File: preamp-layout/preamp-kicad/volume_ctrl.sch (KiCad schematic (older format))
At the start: 64 parts, among them J64 Conn_01x05_Male, J65 Conn_01x02_Male, J66 Conn_01x02_Male, J67 Conn_01x03_Female, J68 Conn_01x03_Female, J69 Conn_01x03_Male, J70 Conn_01x03_Male, J71 Conn_01x03_Male, U10 MCP4902, U11 TL072, U12 TL072, U13 THAT2181, U14 THAT2181, U15 TL072, U16 THAT2181, U17 THAT2181, U18 TL072, U9 MCP4902

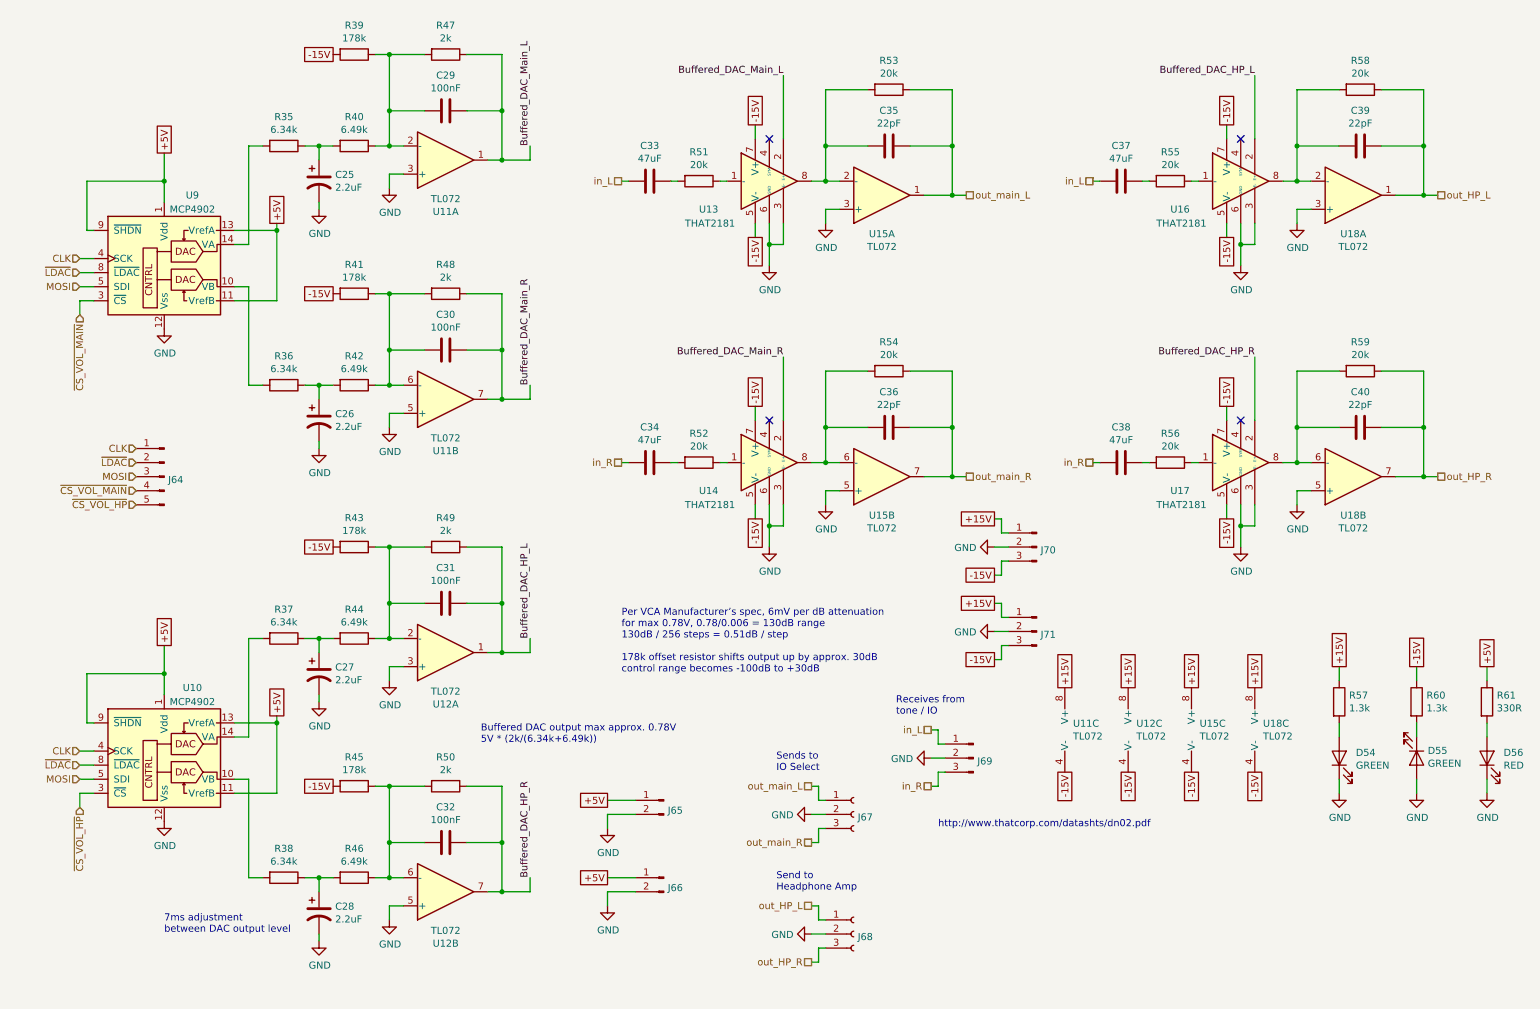
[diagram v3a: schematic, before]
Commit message: Schematic Redesignation
Regenerated RefDes for all parts, updated BOM accordingly and perfomred check on values, RefDes present from schematic to BOM. Value changes, BOM filled in as a result.
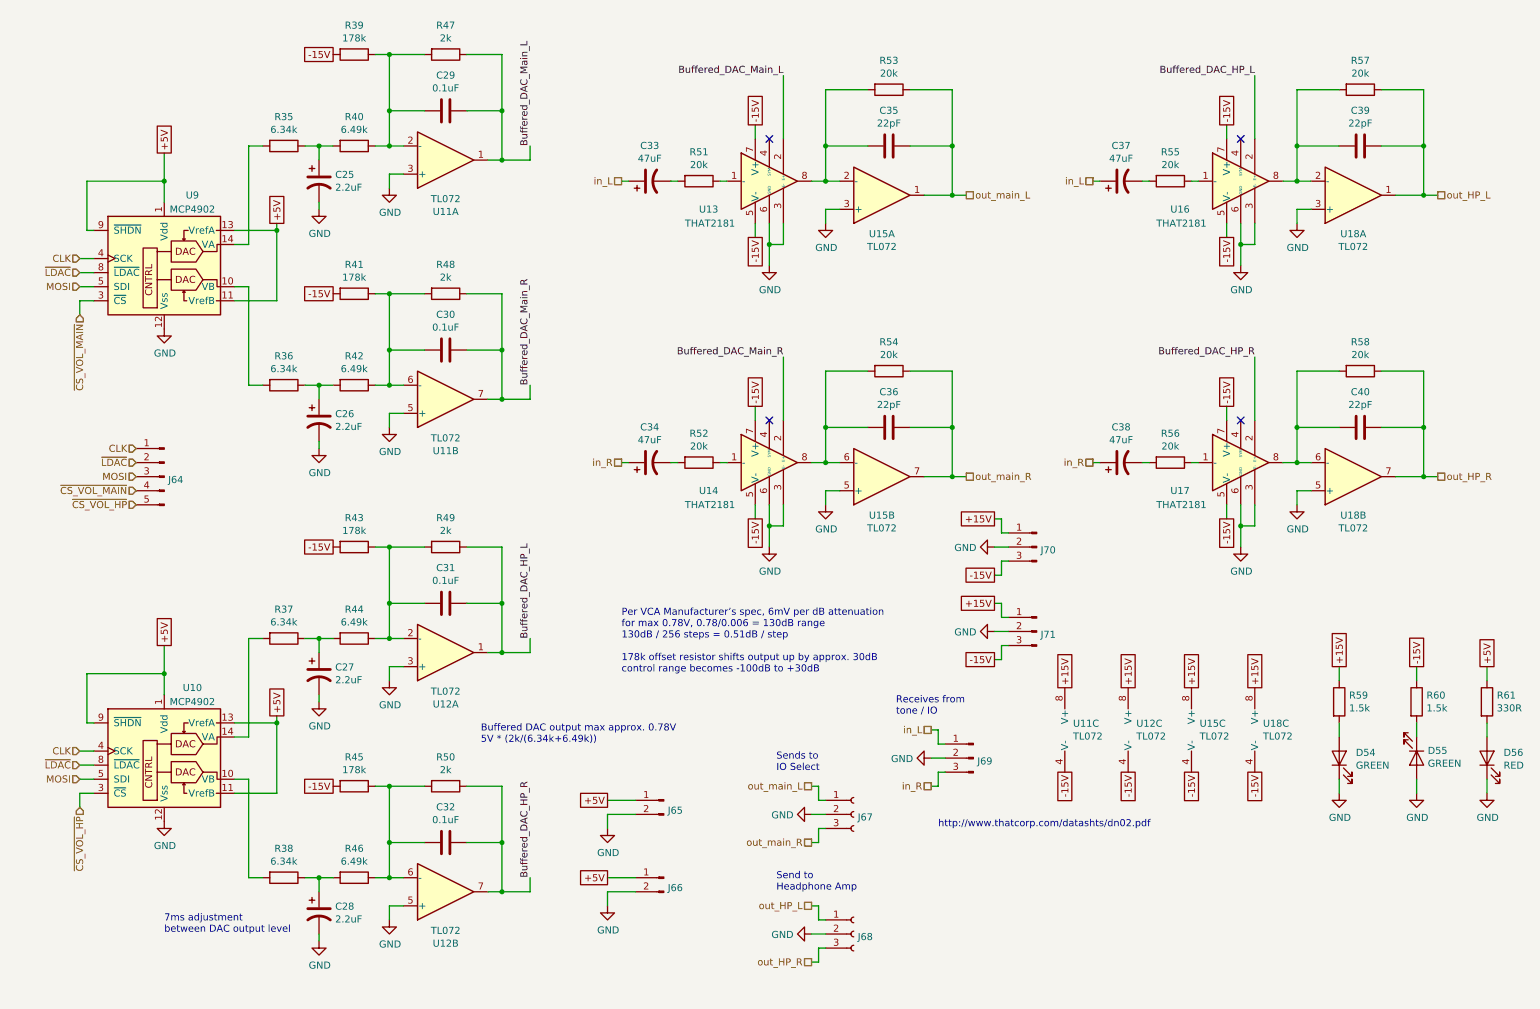
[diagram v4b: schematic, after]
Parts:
- removed C33, C34, C37, C38: 47uF, symbol Device:C
- added C33, C34, C37, C38: 47uF, symbol Device:CP1
- C29, C30, C31, C32: value 100nF -> 0.1uF
- R59: renamed from R57; value 1.3k -> 1.5k
- R60: value 1.3k -> 1.5k
- renumbered R58 to R57, R59 to R58
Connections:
- net in_L: now also C33.1, C37.1
- net in_R: now also C34.1, C38.1
- net at R51.2: now also C33.2
- net at R52.2: now also C34.2
- net at R55.2: now also C37.2
- net at R56.2: now also C38.2
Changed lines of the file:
@@
-	0    1    1    0
-$EndComp
-$Comp
-L Device:C C?
-U 1 1 600B8889
-P 3500 1400
-AR Path="/61DC5D9D/600B8889" Ref="C?"  Part="1"
-AR Path="/5F2E428C/600B8889" Ref="C?"  Part="1"
-AR Path="/61DA059E/600B8889" Ref="C?"  Part="1"
-AR Path="/6009D432/600B8889" Ref="C29"  Part="1"
-F 0 "C29" V 3248 1400 50  0000 C CNN
-F 1 "100nF" V 3339 1400 50  0000 C CNN
-F 2 "Capacitor_SMD:C_0805_2012Metric_Pad1.15x1.40mm_HandSolder" H 3538 1250 50  0001 C CNN
-F 3 "~" H 3500 1400 50  0001 C CNN
-	1    3500 1400
 	0    1    1    0
 $EndComp
@@
 F 3 "~" H 5300 1900 50  0001 C CNN
 	1    5300 1900
-	0    1    1    0
-$EndComp
-$Comp
-L Device:C C?
-U 1 1 60191212
-P 4950 1900
-AR Path="/61DC5D9D/60191212" Ref="C?"  Part="1"
-AR Path="/5F2E428C/60191212" Ref="C?"  Part="1"
-AR Path="/61DA059E/60191212" Ref="C?"  Part="1"
-AR Path="/6009D432/60191212" Ref="C33"  Part="1"
-F 0 "C33" V 4698 1900 50  0000 C CNN
-F 1 "47uF" V 4789 1900 50  0000 C CNN
-F 2 "" H 4988 1750 50  0001 C CNN
-F 3 "~" H 4950 1900 50  0001 C CNN
-	1    4950 1900
 	0    1    1    0
 $EndComp
@@
 AR Path="/6009D432/60205A00" Ref="C30"  Part="1"
 F 0 "C30" V 3248 3100 50  0000 C CNN
-F 1 "100nF" V 3339 3100 50  0000 C CNN
+F 1 "0.1uF" V 3339 3100 50  0000 C CNN
 F 2 "Capacitor_SMD:C_0805_2012Metric_Pad1.15x1.40mm_HandSolder" H 3538 2950 50  0001 C CNN
 F 3 "~" H 3500 3100 50  0001 C CNN
@@
 $EndComp
 $Comp
-L Device:C C?
-U 1 1 602F6E88
-P 4950 3900
-AR Path="/61DC5D9D/602F6E88" Ref="C?"  Part="1"
-AR Path="/5F2E428C/602F6E88" Ref="C?"  Part="1"
-AR Path="/61DA059E/602F6E88" Ref="C?"  Part="1"
-AR Path="/6009D432/602F6E88" Ref="C34"  Part="1"
-F 0 "C34" V 4698 3900 50  0000 C CNN
-F 1 "47uF" V 4789 3900 50  0000 C CNN
-F 2 "" H 4988 3750 50  0001 C CNN
-F 3 "~" H 4950 3900 50  0001 C CNN
-	1    4950 3900
-	0    1    1    0
-$EndComp
-$Comp
 L Amplifier_Audio:THAT2181 U14
 U 1 1 602F6E92
@@
 AR Path="/6009D432/6033B910" Ref="C31"  Part="1"
 F 0 "C31" V 3248 4900 50  0000 C CNN
-F 1 "100nF" V 3339 4900 50  0000 C CNN
+F 1 "0.1uF" V 3339 4900 50  0000 C CNN
 F 2 "Capacitor_SMD:C_0805_2012Metric_Pad1.15x1.40mm_HandSolder" H 3538 4750 50  0001 C CNN
 F 3 "~" H 3500 4900 50  0001 C CNN
@@
 $EndComp
 $Comp
-L Device:C C?
-U 1 1 6033B963
-P 8300 1900
-AR Path="/61DC5D9D/6033B963" Ref="C?"  Part="1"
-AR Path="/5F2E428C/6033B963" Ref="C?"  Part="1"
-AR Path="/61DA059E/6033B963" Ref="C?"  Part="1"
-AR Path="/6009D432/6033B963" Ref="C37"  Part="1"
-F 0 "C37" V 8048 1900 50  0000 C CNN
-F 1 "47uF" V 8139 1900 50  0000 C CNN
-F 2 "" H 8338 1750 50  0001 C CNN
-F 3 "~" H 8300 1900 50  0001 C CNN
-	1    8300 1900
-	0    1    1    0
-$EndComp
-$Comp
 L Amplifier_Audio:THAT2181 U16
 U 1 1 6033B96D
@@
 P 10000 1250
 AR Path="/61DA059E/6033B977" Ref="R?"  Part="1"
-AR Path="/6009D432/6033B977" Ref="R58"  Part="1"
-F 0 "R58" V 9793 1250 50  0000 C CNN
+AR Path="/6009D432/6033B977" Ref="R57"  Part="1"
+F 0 "R57" V 9793 1250 50  0000 C CNN
 F 1 "20k" V 9884 1250 50  0000 C CNN
 F 2 "Resistor_SMD:R_1206_3216Metric_Pad1.42x1.75mm_HandSolder" V 9930 1250 50  0001 C CNN
@@
 AR Path="/6009D432/6033B9D4" Ref="C32"  Part="1"
 F 0 "C32" V 3248 6600 50  0000 C CNN
-F 1 "100nF" V 3339 6600 50  0000 C CNN
+F 1 "0.1uF" V 3339 6600 50  0000 C CNN
 F 2 "Capacitor_SMD:C_0805_2012Metric_Pad1.15x1.40mm_HandSolder" H 3538 6450 50  0001 C CNN
 F 3 "~" H 3500 6600 50  0001 C CNN
@@
 $EndComp
 $Comp
-L Device:C C?
-U 1 1 6033BA6E
-P 8300 3900
-AR Path="/61DC5D9D/6033BA6E" Ref="C?"  Part="1"
-AR Path="/5F2E428C/6033BA6E" Ref="C?"  Part="1"
-AR Path="/61DA059E/6033BA6E" Ref="C?"  Part="1"
-AR Path="/6009D432/6033BA6E" Ref="C38"  Part="1"
-F 0 "C38" V 8048 3900 50  0000 C CNN
-F 1 "47uF" V 8139 3900 50  0000 C CNN
-F 2 "" H 8338 3750 50  0001 C CNN
-F 3 "~" H 8300 3900 50  0001 C CNN
-	1    8300 3900
-	0    1    1    0
-$EndComp
-$Comp
 L Amplifier_Audio:THAT2181 U17
 U 1 1 6033BA78
@@
 P 10000 3250
 AR Path="/61DA059E/6033BA82" Ref="R?"  Part="1"
-AR Path="/6009D432/6033BA82" Ref="R59"  Part="1"
-F 0 "R59" V 9793 3250 50  0000 C CNN
+AR Path="/6009D432/6033BA82" Ref="R58"  Part="1"
+F 0 "R58" V 9793 3250 50  0000 C CNN
 F 1 "20k" V 9884 3250 50  0000 C CNN
 F 2 "Resistor_SMD:R_1206_3216Metric_Pad1.42x1.75mm_HandSolder" V 9930 3250 50  0001 C CNN
@@
 AR Path="/6072D4FD" Ref="R?"  Part="1"
 AR Path="/5E27B612/6072D4FD" Ref="R?"  Part="1"
-AR Path="/6009D432/6072D4FD" Ref="R57"  Part="1"
-F 0 "R57" H 9920 5646 50  0000 L CNN
-F 1 "1.3k" H 9920 5555 50  0000 L CNN
+AR Path="/6009D432/6072D4FD" Ref="R59"  Part="1"
+F 0 "R59" H 9920 5646 50  0000 L CNN
+F 1 "1.5k" H 9920 5555 50  0000 L CNN
 F 2 "Resistor_SMD:R_1206_3216Metric_Pad1.42x1.75mm_HandSolder" V 9780 5600 50  0001 C CNN
 F 3 "~" H 9850 5600 50  0001 C CNN
@@
 AR Path="/6009D432/6072D50D" Ref="R60"  Part="1"
 F 0 "R60" H 10470 5646 50  0000 L CNN
-F 1 "1.3k" H 10470 5555 50  0000 L CNN
+F 1 "1.5k" H 10470 5555 50  0000 L CNN
 F 2 "Resistor_SMD:R_1206_3216Metric_Pad1.42x1.75mm_HandSolder" V 10330 5600 50  0001 C CNN
 F 3 "~" H 10400 5600 50  0001 C CNN
@@
 Wire Wire Line
 	900  2750 1000 2750
+$Comp
+L Device:C C?
+U 1 1 600B8889
+P 3500 1400
+AR Path="/61DC5D9D/600B8889" Ref="C?"  Part="1"
+AR Path="/5F2E428C/600B8889" Ref="C?"  Part="1"
+AR Path="/61DA059E/600B8889" Ref="C?"  Part="1"
+AR Path="/6009D432/600B8889" Ref="C29"  Part="1"
+F 0 "C29" V 3248 1400 50  0000 C CNN
+F 1 "0.1uF" V 3339 1400 50  0000 C CNN
+F 2 "Capacitor_SMD:C_0805_2012Metric_Pad1.15x1.40mm_HandSolder" H 3538 1250 50  0001 C CNN
+F 3 "~" H 3500 1400 50  0001 C CNN
+	1    3500 1400
+	0    1    1    0
+$EndComp
+$Comp
+L Device:CP1 C34
+U 1 1 5EE7EEA5
+P 4950 3900
+F 0 "C34" V 5202 3900 50  0000 C CNN
+F 1 "47uF" V 5111 3900 50  0000 C CNN
+F 2 "" H 4950 3900 50  0001 C CNN
+F 3 "~" H 4950 3900 50  0001 C CNN
+	1    4950 3900
+	0    -1   -1   0
+$EndComp
+$Comp
+L Device:CP1 C33
+U 1 1 5EED08EE
+P 4950 1900
+F 0 "C33" V 5202 1900 50  0000 C CNN
+F 1 "47uF" V 5111 1900 50  0000 C CNN
+F 2 "" H 4950 1900 50  0001 C CNN
+F 3 "~" H 4950 1900 50  0001 C CNN
+	1    4950 1900
+	0    -1   -1   0
+$EndComp
+$Comp
+L Device:CP1 C38
+U 1 1 5EEE50A1
+P 8300 3900
+F 0 "C38" V 8552 3900 50  0000 C CNN
+F 1 "47uF" V 8461 3900 50  0000 C CNN
+F 2 "" H 8300 3900 50  0001 C CNN
+F 3 "~" H 8300 3900 50  0001 C CNN
+	1    8300 3900
+	0    -1   -1   0
+$EndComp
+$Comp
+L Device:CP1 C37
+U 1 1 5EEE50AB
+P 8300 1900
+F 0 "C37" V 8552 1900 50  0000 C CNN
+F 1 "47uF" V 8461 1900 50  0000 C CNN
+F 2 "" H 8300 1900 50  0001 C CNN
+F 3 "~" H 8300 1900 50  0001 C CNN
+	1    8300 1900
+	0    -1   -1   0
+$EndComp
 $EndSCHEMATC

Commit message: Added Bypass Capacitors
0.1uF caps added at power supplies of all ICs
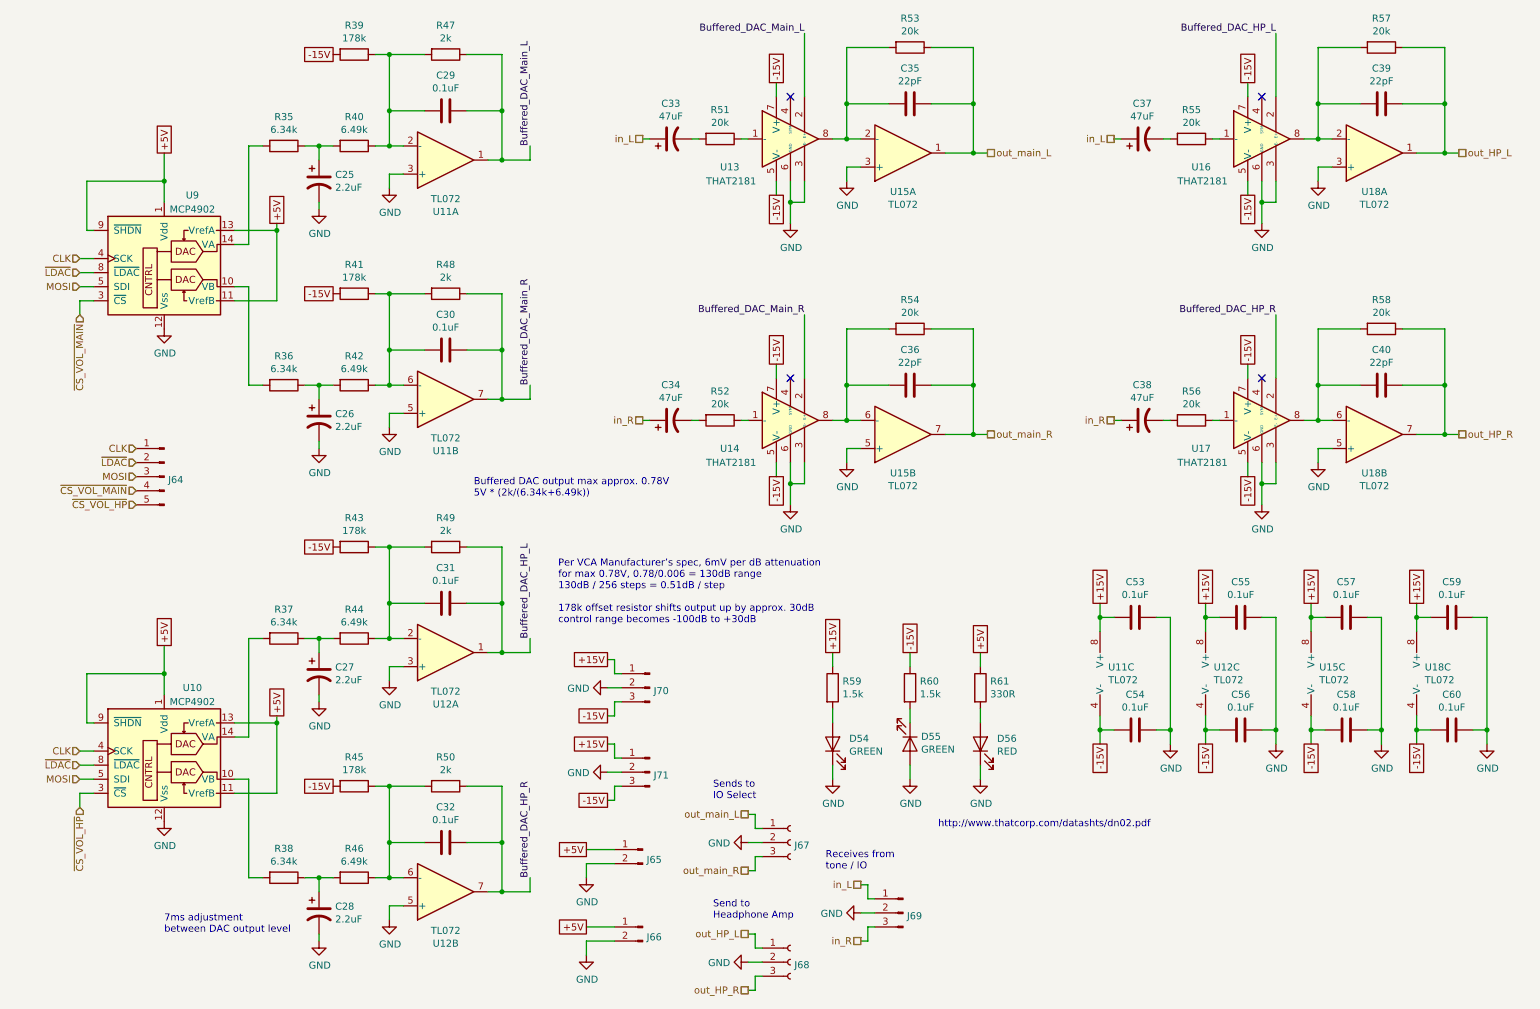
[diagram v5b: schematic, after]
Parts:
- added C53, C54, C55, C56, C57, C58, C59, C60: 0.1uF, Capacitor_SMD:C_0805_2012Metric_Pad1.15x1.40mm_HandSolder, symbol Device:C
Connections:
- net +15V: now also C53.1, C55.1, C57.1, C59.1
- net -15V: now also C54.1, C56.1, C58.1, C60.1
- net GND: now also C53.2, C54.2, C55.2, C56.2, C57.2, C58.2, C59.2, C60.2
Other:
- moved on the sheet: C33, C34, C35, C36, C37, C38, C39, C40, D54, D55, D56, J65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

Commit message: Footprint assignment updates
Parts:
- U11, U12, U15, U18: footprint (none) -> Package_DIP:DIP-8_W7.62mm_Socket_LongPads
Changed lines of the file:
@@
 F 0 "U11" H 8208 5446 50  0000 L CNN
 F 1 "TL072" H 8208 5355 50  0000 L CNN
-F 2 "" H 8250 5400 50  0001 C CNN
+F 2 "Package_DIP:DIP-8_W7.62mm_Socket_LongPads" H 8250 5400 50  0001 C CNN
 F 3 "http://www.ti.com/lit/ds/symlink/tl071.pdf" H 8250 5400 50  0001 C CNN
 	3    8250 5400
@@
 F 0 "U12" H 8958 5446 50  0000 L CNN
 F 1 "TL072" H 8958 5355 50  0000 L CNN
-F 2 "" H 9000 5400 50  0001 C CNN
+F 2 "Package_DIP:DIP-8_W7.62mm_Socket_LongPads" H 9000 5400 50  0001 C CNN
 F 3 "http://www.ti.com/lit/ds/symlink/tl071.pdf" H 9000 5400 50  0001 C CNN
 	3    9000 5400
@@
 F 0 "U15" H 9708 5446 50  0000 L CNN
 F 1 "TL072" H 9708 5355 50  0000 L CNN
-F 2 "" H 9750 5400 50  0001 C CNN
+F 2 "Package_DIP:DIP-8_W7.62mm_Socket_LongPads" H 9750 5400 50  0001 C CNN
 F 3 "http://www.ti.com/lit/ds/symlink/tl071.pdf" H 9750 5400 50  0001 C CNN
 	3    9750 5400
@@
 F 0 "U18" H 10458 5446 50  0000 L CNN
 F 1 "TL072" H 10458 5355 50  0000 L CNN
-F 2 "" H 10500 5400 50  0001 C CNN
+F 2 "Package_DIP:DIP-8_W7.62mm_Socket_LongPads" H 10500 5400 50  0001 C CNN
 F 3 "http://www.ti.com/lit/ds/symlink/tl071.pdf" H 10500 5400 50  0001 C CNN
 	3    10500 5400
